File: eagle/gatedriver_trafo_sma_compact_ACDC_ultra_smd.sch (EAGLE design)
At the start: 88 parts, among them K1 G5V-2, X4 BU-SMA-V

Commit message: submit smd board
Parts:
- added GND, GND15: TPPAD1-20Y, testpad:TPPAD1-20Y
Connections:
- net GND: now also GND.TP, GND15.TP
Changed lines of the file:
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@@
 <part name="D24" library="diode" deviceset="DIODE-" device="SMB"/>
 <part name="D25" library="diode" deviceset="DIODE-" device="SMB"/>
+<part name="GND" library="testpad" deviceset="TP" device="PAD1-20Y"/>
+<part name="GND13" library="supply1" deviceset="GND" device=""/>
+<part name="GND15" library="testpad" deviceset="TP" device="PAD1-20Y"/>
+<part name="GND16" library="supply1" deviceset="GND" device=""/>
 </parts>
 <sheets>
@@
 <instance part="D24" gate="G$1" x="78.74" y="-58.42" rot="R180"/>
 <instance part="D25" gate="G$1" x="78.74" y="-81.28" rot="R180"/>
+<instance part="GND" gate="G$1" x="101.6" y="101.6" rot="MR0"/>
+<instance part="GND13" gate="1" x="101.6" y="96.52"/>
+<instance part="GND15" gate="G$1" x="114.3" y="101.6" rot="MR0"/>
+<instance part="GND16" gate="1" x="114.3" y="96.52"/>
 </instances>
 <busses>
@@
 <pinref part="GND14" gate="1" pin="GND"/>
 </segment>
+<segment>
+<pinref part="GND" gate="G$1" pin="TP"/>
+<pinref part="GND13" gate="1" pin="GND"/>
+</segment>
+<segment>
+<pinref part="GND15" gate="G$1" pin="TP"/>
+<pinref part="GND16" gate="1" pin="GND"/>
+</segment>
 </net>

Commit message: Fix negative rail problems
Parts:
- D14, D16, D17, D2, D22, D23, D5, D6: value 4742 -> 1SMB5918BT3G
- R10, R11, R15, R16, R22, R23, R4, R7: value 1M -> 10M
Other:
- moved on the sheet: D11, K1

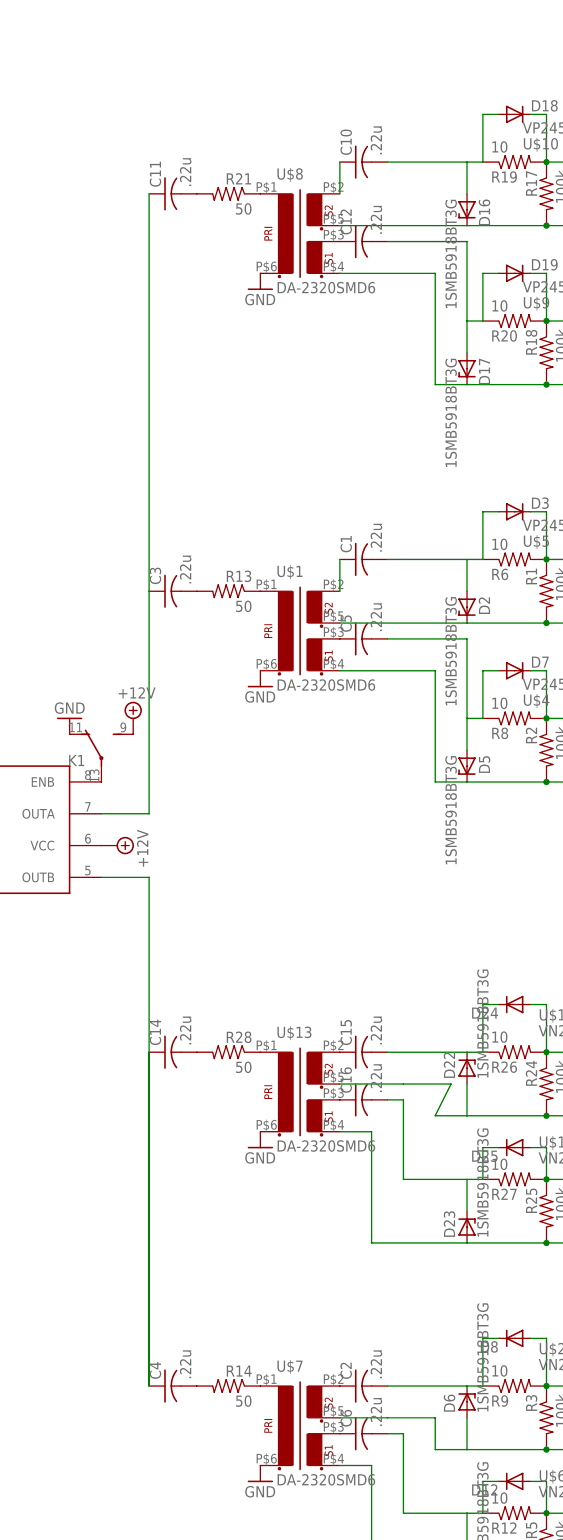
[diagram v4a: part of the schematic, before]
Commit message: Component value changes for gate driver with new fets (VN2450)
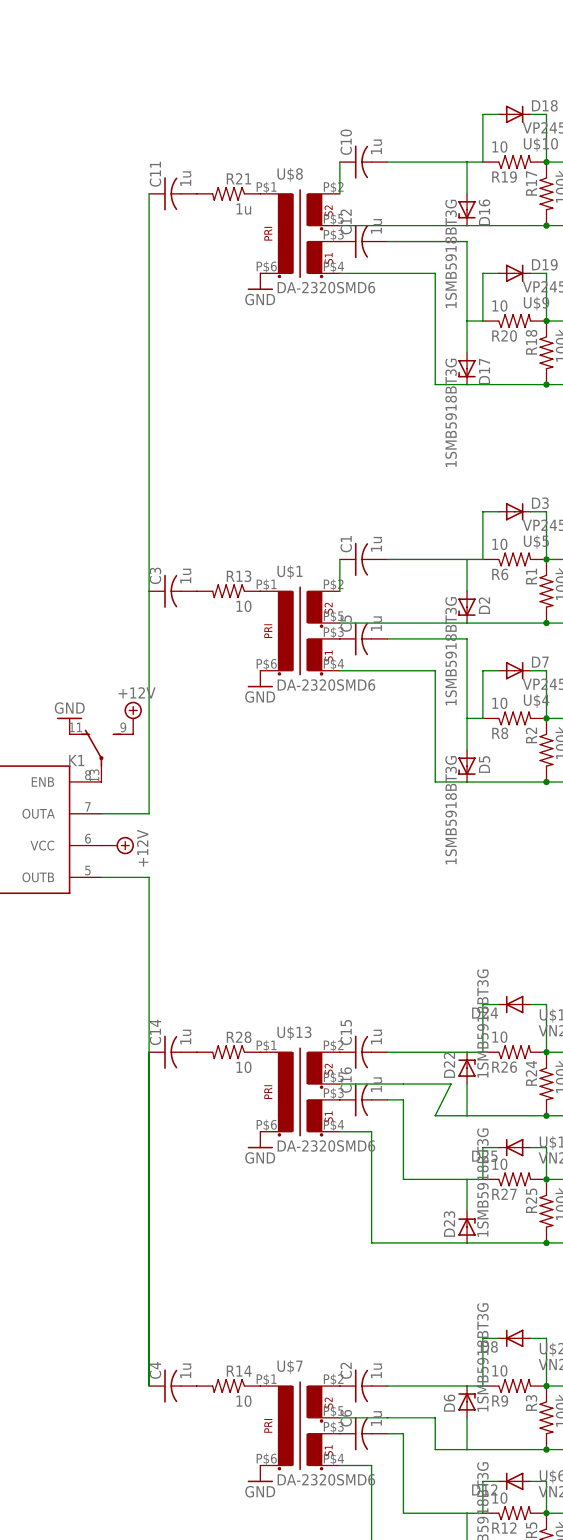
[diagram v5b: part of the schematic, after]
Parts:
- C1, C10, C11, C12, C14, C15, C16, C2, C3, C4, C5, C6: value .22u -> 1u
- R13, R14, R28: value 50 -> 10
- R21: value 50 -> 1u

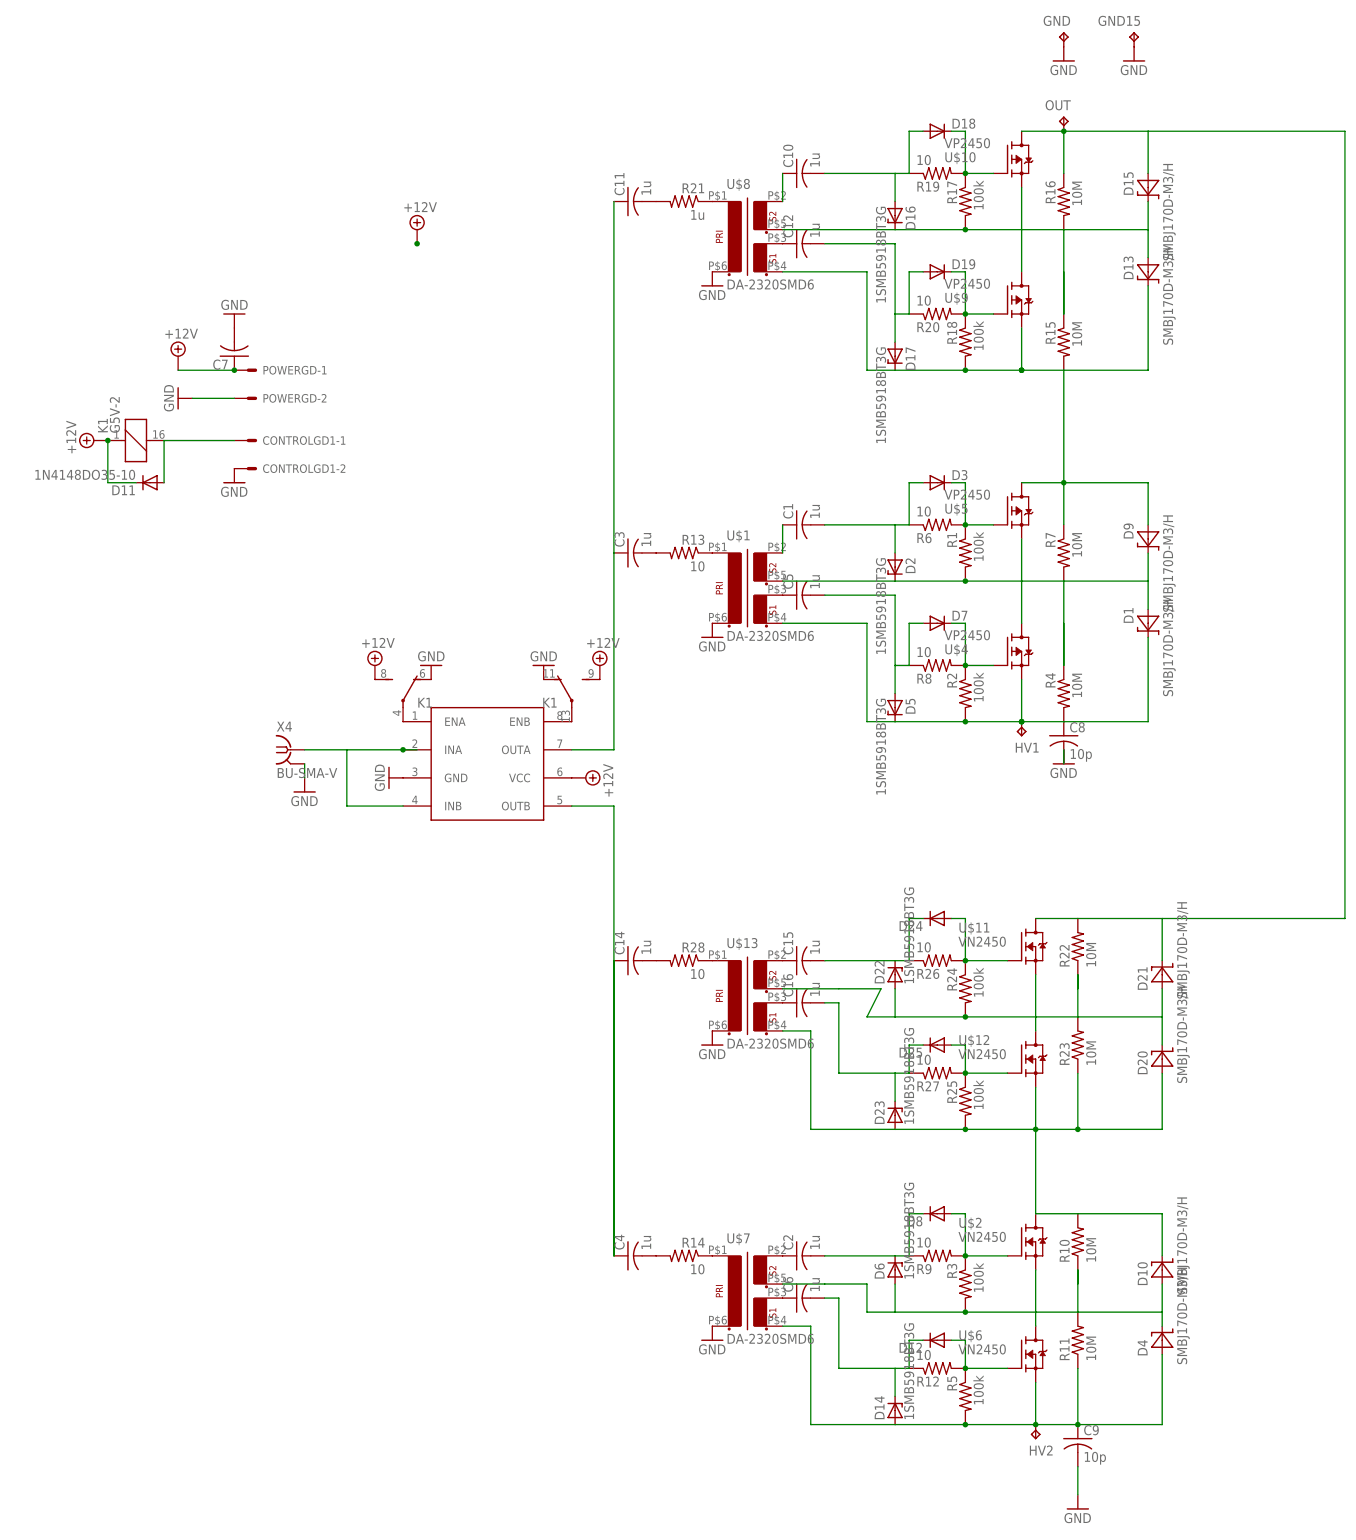
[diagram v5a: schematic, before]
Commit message: Changes for CTIA integration
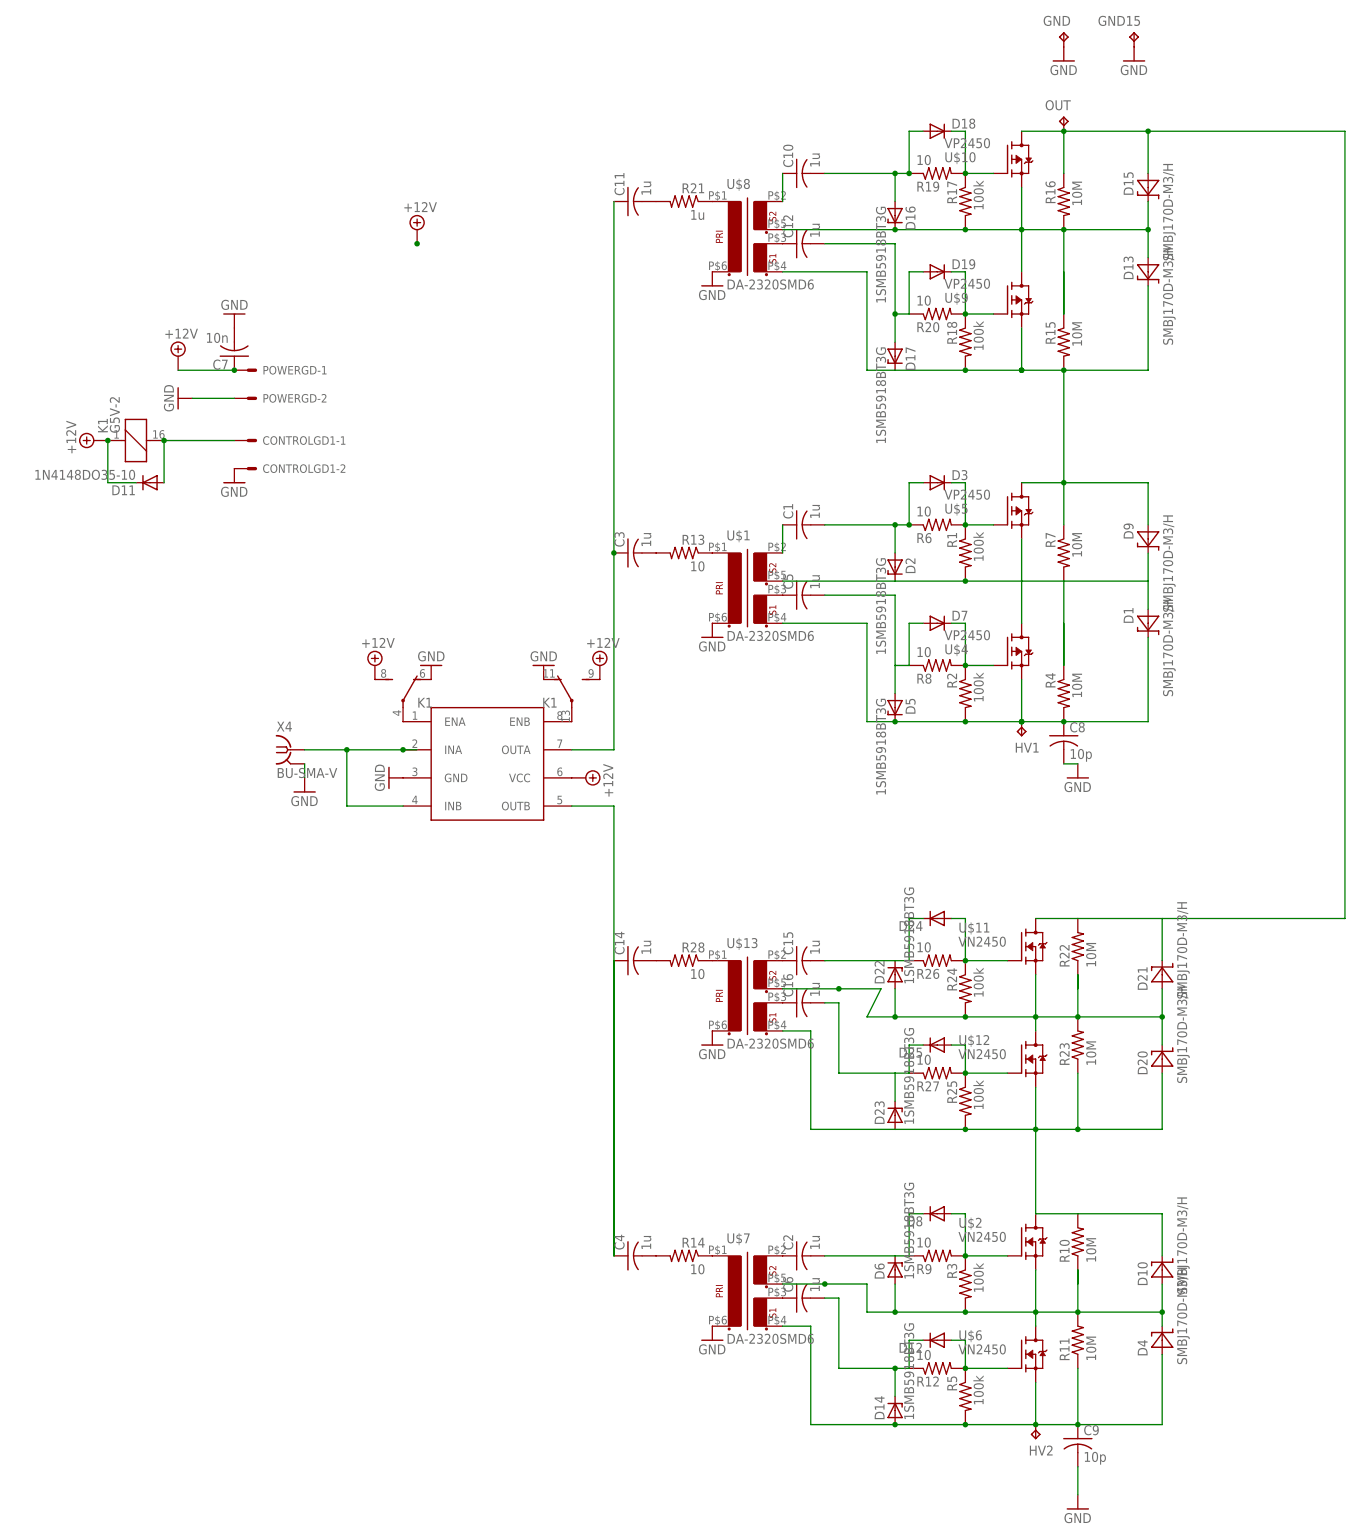
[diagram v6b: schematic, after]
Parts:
- C7: value (none) -> 10n
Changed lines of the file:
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@@
 <part name="D6" library="diode" deviceset="ZENER-DIODE" device="SMB" value="1SMB5918BT3G"/>
 <part name="D14" library="diode" deviceset="ZENER-DIODE" device="SMB" value="1SMB5918BT3G"/>
-<part name="C7" library="rcl" deviceset="C-US" device="050-030X075"/>
+<part name="C7" library="rcl" deviceset="C-US" device="050-030X075" value="10n"/>
 <part name="GND4" library="supply1" deviceset="GND" device=""/>
 <part name="R1" library="rcl" deviceset="R-US_" device="R0805" value="100k"/>
@@
 <instance part="R14" gate="G$1" x="33.02" y="-119.38" rot="MR0"/>
 <instance part="C8" gate="G$1" x="101.6" y="-25.4"/>
-<instance part="GND11" gate="1" x="101.6" y="-30.48"/>
+<instance part="GND11" gate="1" x="104.14" y="-33.02"/>
 <instance part="HV2" gate="G$1" x="96.52" y="-152.4" rot="MR180"/>
 <instance part="C9" gate="G$1" x="104.14" y="-152.4"/>
@@
 <pinref part="C8" gate="G$1" pin="2"/>
 <pinref part="GND11" gate="1" pin="GND"/>
-<wire x1="101.6" y1="-30.48" x2="101.6" y2="-27.94" width="0.1524" layer="91"/>
+<wire x1="101.6" y1="-30.48" x2="104.14" y2="-30.48" width="0.1524" layer="91"/>
 </segment>
 <segment>
@@
 <pinref part="U$3" gate="G$1" pin="INA"/>
 <junction x="-17.78" y="-27.94"/>
+<junction x="-27.94" y="-27.94"/>
 </segment>
 </net>
@@
 <pinref part="U$3" gate="G$1" pin="OUTA"/>
 <wire x1="20.32" y1="-27.94" x2="12.7" y2="-27.94" width="0.1524" layer="91"/>
-</segment>
-<segment>
 <pinref part="C11" gate="G$1" pin="1"/>
 <wire x1="20.32" y1="71.12" x2="20.32" y2="7.62" width="0.1524" layer="91"/>
+<junction x="20.32" y="7.62"/>
 </segment>
 </net>
@@
 <wire x1="-60.96" y1="20.32" x2="-60.96" y2="27.94" width="0.1524" layer="91"/>
 <pinref part="D11" gate="G$1" pin="A"/>
+<junction x="-60.96" y="27.94"/>
 </segment>
 </net>
@@
 <wire x1="76.2" y1="-134.62" x2="73.66" y2="-134.62" width="0.1524" layer="91"/>
 <wire x1="73.66" y1="-134.62" x2="73.66" y2="-139.7" width="0.1524" layer="91"/>
+<junction x="71.12" y="-139.7"/>
 </segment>
 </net>
@@
 <junction x="83.82" y="-22.86"/>
 <wire x1="93.98" y1="-22.86" x2="101.6" y2="-22.86" width="0.1524" layer="91"/>
+<junction x="101.6" y="-22.86"/>
+<junction x="71.12" y="-22.86"/>
 </segment>
 </net>
@@
 <pinref part="R3" gate="G$1" pin="2"/>
 <junction x="83.82" y="-129.54"/>
-</segment>
-<segment>
 <pinref part="U$7" gate="G$1" pin="5"/>
 <wire x1="50.8" y1="-124.46" x2="58.42" y2="-124.46" width="0.1524" layer="91"/>
+<junction x="58.42" y="-124.46"/>
+<junction x="96.52" y="-129.54"/>
+<junction x="71.12" y="-129.54"/>
+<junction x="119.38" y="-129.54"/>
+<junction x="104.14" y="-129.54"/>
 </segment>
 </net>
@@
 <wire x1="76.2" y1="20.32" x2="73.66" y2="20.32" width="0.1524" layer="91"/>
 <wire x1="73.66" y1="20.32" x2="73.66" y2="12.7" width="0.1524" layer="91"/>
+<junction x="73.66" y="12.7"/>
+<junction x="71.12" y="12.7"/>
 </segment>
 </net>
@@
 <pinref part="C9" gate="G$1" pin="1"/>
 <junction x="104.14" y="-149.86"/>
+<junction x="71.12" y="-149.86"/>
 </segment>
 </net>
@@
 <wire x1="76.2" y1="58.42" x2="73.66" y2="58.42" width="0.1524" layer="91"/>
 <wire x1="73.66" y1="58.42" x2="73.66" y2="50.8" width="0.1524" layer="91"/>
+<junction x="71.12" y="50.8"/>
 </segment>
 </net>
@@
 <pinref part="R17" gate="G$1" pin="2"/>
 <junction x="83.82" y="66.04"/>
+<junction x="101.6" y="66.04"/>
+<junction x="93.98" y="66.04"/>
+<junction x="116.84" y="66.04"/>
+<junction x="71.12" y="66.04"/>
 </segment>
 </net>
@@
 <wire x1="76.2" y1="83.82" x2="73.66" y2="83.82" width="0.1524" layer="91"/>
 <wire x1="73.66" y1="83.82" x2="73.66" y2="76.2" width="0.1524" layer="91"/>
+<junction x="73.66" y="76.2"/>
+<junction x="71.12" y="76.2"/>
 </segment>
 </net>
@@
 <pinref part="R24" gate="G$1" pin="2"/>
 <junction x="83.82" y="-76.2"/>
-</segment>
-<segment>
 <pinref part="U$13" gate="G$1" pin="5"/>
 <wire x1="50.8" y1="-71.12" x2="60.96" y2="-71.12" width="0.1524" layer="91"/>
+<junction x="60.96" y="-71.12"/>
+<junction x="104.14" y="-76.2"/>
+<junction x="119.38" y="-76.2"/>
+<junction x="96.52" y="-76.2"/>
+<junction x="71.12" y="-76.2"/>
 </segment>
 </net>
@@
 <wire x1="152.4" y1="83.82" x2="152.4" y2="-58.42" width="0.1524" layer="91"/>
 <wire x1="116.84" y1="83.82" x2="152.4" y2="83.82" width="0.1524" layer="91"/>
+<junction x="116.84" y="83.82"/>
 </segment>
 </net>
@@
 <wire x1="93.98" y1="40.64" x2="101.6" y2="40.64" width="0.1524" layer="91"/>
 <wire x1="101.6" y1="20.32" x2="101.6" y2="40.64" width="0.1524" layer="91"/>
-</segment>
-</net>
+<junction x="101.6" y="40.64"/>
+</segment>
+</net>
